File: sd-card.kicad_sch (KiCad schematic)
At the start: 2 parts, among them J7 Micro-SD-card

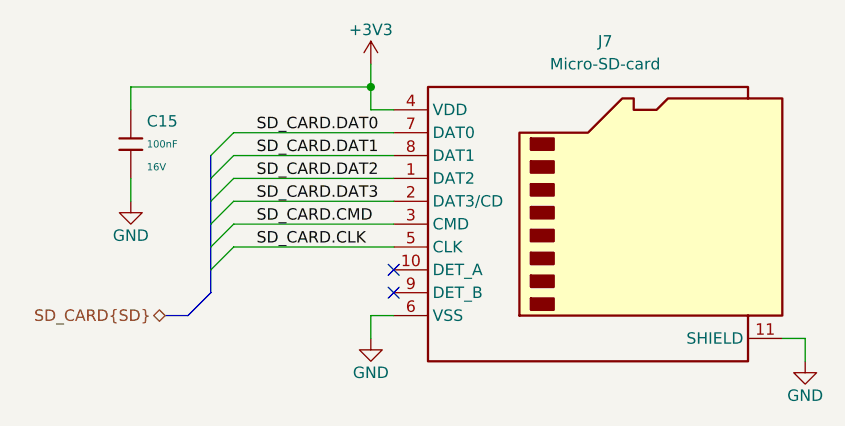
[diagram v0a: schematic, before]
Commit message: [#1] WIP: Change components to ones from the global library, refactor schematic
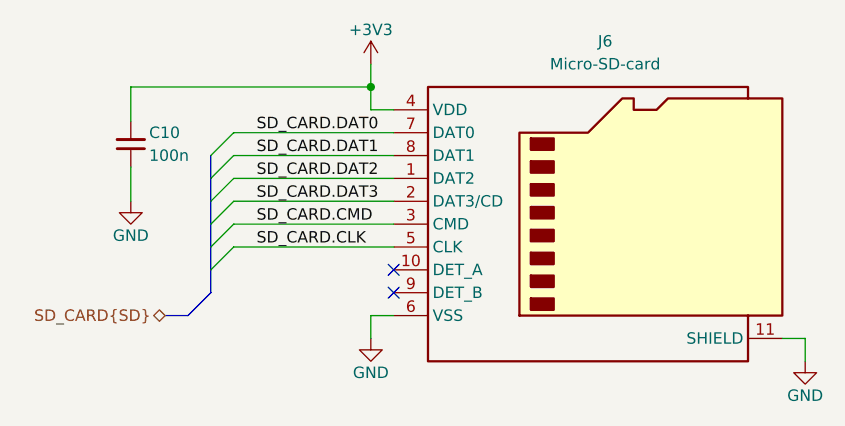
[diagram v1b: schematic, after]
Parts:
- removed C15: 100nF, PCM_JLCPCB:C_0402, symbol PCM_JLCPCB-Capacitors:0402,100nF
- added C10: C-100n-0402, DW-footprints:C_0402_1005Metric, symbol DW-capacitors:C-100n-0402
- renumbered J7 to J6
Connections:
- net +3V3: now also C10.2
- net GND: now also C10.1
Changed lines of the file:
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@@
 	(wire
 		(pts
-			(xy 142.24 113.03) (xy 142.24 115.57)
+			(xy 142.24 113.03) (xy 142.24 116.84)
 		)
 		(stroke
@@
 		)
 	)
+	(wire
+		(pts
+			(xy 142.24 121.92) (xy 142.24 125.73)
+		)
+		(stroke
+			(width 0)
+			(type default)
+		)
+	)
 	(bus
 		(pts
@@
 		(pts
 			(xy 171.45 115.57) (xy 168.91 115.57)
-		)
-		(stroke
-			(width 0)
-			(type default)
-		)
-	)
-	(wire
-		(pts
-			(xy 142.24 123.19) (xy 142.24 125.73)
 		)
 		(stroke
@@
 			)
 			(justify right)
+		)
+	)
+	(symbol
+		(lib_id "DW-capacitors:C-100n-0402")
+		(at 142.24 121.92 90)
+		(unit 1)
+		(exclude_from_sim no)
+		(in_bom yes)
+		(on_board yes)
+		(dnp no)
+		(property "Reference" "C10"
+			(at 144.272 118.11 90)
+			(effects
+				(font
+					(size 1.27 1.27)
+					(thickness 0.15)
+				)
+				(justify right)
+			)
+		)
+		(property "Value" "C-100n-0402"
+			(at 144.78 109.22 0)
+			(effects
+				(font
+					(size 1.27 1.27)
+					(thickness 0.15)
+				)
+				(justify left bottom)
+				(hide yes)
+			)
+		)
+		(property "Footprint" "DW-footprints:C_0402_1005Metric"
+			(at 147.32 109.22 0)
+			(effects
+				(font
+					(size 1.27 1.27)
+					(thickness 0.15)
+				)
+				(justify left bottom)
+				(hide yes)
+			)
+		)
+		(property "Datasheet" "https://lcsc.com/datasheet/lcsc_datasheet_2304140030_Samsung-Electro-Mechanics-CL05B104KB54PNC_C307331.pdf"
+			(at 149.86 109.22 0)
+			(effects
+				(font
+					(size 1.27 1.27)
+					(thickness 0.15)
+				)
+				(justify left bottom)
+				(hide yes)
+			)
+		)
+		(property "Description" "50V 100nF X7R ±10% 0402 Multilayer Ceramic Capacitors MLCC - SMD/SMT ROHS"
+			(at 152.4 109.22 0)
+			(effects
+				(font
+					(size 1.27 1.27)
+					(thickness 0.15)
+				)
+				(justify left bottom)
+				(hide yes)
+			)
+		)
+		(property "Manufacturer" "Samsung Electro-Mechanics"
+			(at 154.94 109.22 0)
+			(effects
+				(font
+					(size 1.27 1.27)
+					(thickness 0.15)
+				)
+				(justify left bottom)
+				(hide yes)
+			)
+		)
+		(property "MPN" "CL05B104KB54PNC"
+			(at 157.48 109.22 0)
+			(effects
+				(font
+					(size 1.27 1.27)
+					(thickness 0.15)
+				)
+				(justify left bottom)
+				(hide yes)
+			)
+		)
+		(property "LCSC" "C307331"
+			(at 160.02 109.22 0)
+			(effects
+				(font
+					(size 1.27 1.27)
+					(thickness 0.15)
+				)
+				(justify left bottom)
+				(hide yes)
+			)
+		)
+		(property "Val" "100n"
+			(at 144.272 120.65 90)
+			(effects
+				(font
+					(size 1.27 1.27)
+					(thickness 0.15)
+				)
+				(justify right)
+			)
+		)
+		(property "Tolerance" "10%"
+			(at 165.1 109.22 0)
+			(effects
+				(font
+					(size 1.27 1.27)
+					(thickness 0.15)
+				)
+				(justify left bottom)
+				(hide yes)
+			)
+		)
+		(property "Voltage" "50V"
+			(at 167.64 109.22 0)
+			(effects
+				(font
+					(size 1.27 1.27)
+					(thickness 0.15)
+				)
+				(justify left bottom)
+				(hide yes)
+			)
+		)
+		(property "Dielectric" "X7R"
+			(at 170.18 109.22 0)
+			(effects
+				(font
+					(size 1.27 1.27)
+					(thickness 0.15)
+				)
+				(justify left bottom)
+				(hide yes)
+			)
+		)
+		(pin "1"
+		)
+		(pin "2"
+		)
+		(instances
+			(project ""
+				(path "/090a8e41-87a8-4fb1-998b-60a2c0dc4cee/df5d742e-fec8-4307-bd86-008404d5e8ea"
+					(reference "C10")
+					(unit 1)
+				)
+			)
 		)
 	)
@@
 		(on_board yes)
 		(dnp no)
-		(property "Reference" "#PWR066"
+		(property "Reference" "#PWR052"
 			(at 217.17 149.86 0)
 			(effects
@@
 			(project "cm5-module"
 				(path "/090a8e41-87a8-4fb1-998b-60a2c0dc4cee/df5d742e-fec8-4307-bd86-008404d5e8ea"
-					(reference "#PWR066")
+					(reference "#PWR052")
 					(unit 1)
 				)
@@
 		(on_board yes)
 		(dnp no)
-		(property "Reference" "#PWR068"
+		(property "Reference" "#PWR049"
 			(at 168.91 114.3 0)
 			(effects
@@
 			(project "cm5-module"
 				(path "/090a8e41-87a8-4fb1-998b-60a2c0dc4cee/df5d742e-fec8-4307-bd86-008404d5e8ea"
-					(reference "#PWR068")
+					(reference "#PWR049")
 					(unit 1)
 				)
@@
 		(on_board yes)
 		(dnp no)
-		(property "Reference" "#PWR067"
+		(property "Reference" "#PWR051"
 			(at 168.91 147.32 0)
 			(effects
@@
 			(project "cm5-module"
 				(path "/090a8e41-87a8-4fb1-998b-60a2c0dc4cee/df5d742e-fec8-4307-bd86-008404d5e8ea"
-					(reference "#PWR067")
+					(reference "#PWR051")
 					(unit 1)
 				)
@@
 		(dnp no)
 		(fields_autoplaced yes)
-		(property "Reference" "J7"
+		(property "Reference" "J6"
 			(at 194.945 107.95 0)
 			(effects
@@
 			(project ""
 				(path "/090a8e41-87a8-4fb1-998b-60a2c0dc4cee/df5d742e-fec8-4307-bd86-008404d5e8ea"
-					(reference "J7")
-					(unit 1)
-				)
-			)
-		)
-	)
-	(symbol
-		(lib_id "PCM_JLCPCB-Capacitors:0402,100nF")
-		(at 142.24 119.38 0)
-		(unit 1)
-		(exclude_from_sim no)
-		(in_bom yes)
-		(on_board yes)
-		(dnp no)
-		(property "Reference" "C15"
-			(at 144.018 116.8399 0)
-			(effects
-				(font
-					(size 1.27 1.27)
-				)
-				(justify left)
-			)
-		)
-		(property "Value" "100nF"
-			(at 144.018 119.38 0)
-			(effects
-				(font
-					(size 0.8 0.8)
-				)
-				(justify left)
-			)
-		)
-		(property "Footprint" "PCM_JLCPCB:C_0402"
-			(at 140.462 119.38 90)
-			(effects
-				(font
-					(size 1.27 1.27)
-				)
-				(hide yes)
-			)
-		)
-		(property "Datasheet" "https://www.lcsc.com/datasheet/lcsc_datasheet_2304140030_Samsung-Electro-Mechanics-CL05B104KO5NNNC_C1525.pdf"
-			(at 142.24 119.38 0)
-			(effects
-				(font
-					(size 1.27 1.27)
-				)
-				(hide yes)
-			)
-		)
-		(property "Description" "16V 100nF X7R ±10% 0402 Multilayer Ceramic Capacitors MLCC - SMD/SMT ROHS"
-			(at 142.24 119.38 0)
-			(effects
-				(font
-					(size 1.27 1.27)
-				)
-				(hide yes)
-			)
-		)
-		(property "LCSC" "C1525"
-			(at 142.24 119.38 0)
-			(effects
-				(font
-					(size 1.27 1.27)
-				)
-				(hide yes)
-			)
-		)
-		(property "Stock" "17504271"
-			(at 142.24 119.38 0)
-			(effects
-				(font
-					(size 1.27 1.27)
-				)
-				(hide yes)
-			)
-		)
-		(property "Price" "0.004USD"
-			(at 142.24 119.38 0)
-			(effects
-				(font
-					(size 1.27 1.27)
-				)
-				(hide yes)
-			)
-		)
-		(property "Process" "SMT"
-			(at 142.24 119.38 0)
-			(effects
-				(font
-					(size 1.27 1.27)
-				)
-				(hide yes)
-			)
-		)
-		(property "Minimum Qty" "20"
-			(at 142.24 119.38 0)
-			(effects
-				(font
-					(size 1.27 1.27)
-				)
-				(hide yes)
-			)
-		)
-		(property "Attrition Qty" "10"
-			(at 142.24 119.38 0)
-			(effects
-				(font
-					(size 1.27 1.27)
-				)
-				(hide yes)
-			)
-		)
-		(property "Class" "Basic Component"
-			(at 142.24 119.38 0)
-			(effects
-				(font
-					(size 1.27 1.27)
-				)
-				(hide yes)
-			)
-		)
-		(property "Category" "Capacitors,Multilayer Ceramic Capacitors MLCC - SMD/SMT"
-			(at 142.24 119.38 0)
-			(effects
-				(font
-					(size 1.27 1.27)
-				)
-				(hide yes)
-			)
-		)
-		(property "Manufacturer" "Samsung Electro-Mechanics"
-			(at 142.24 119.38 0)
-			(effects
-				(font
-					(size 1.27 1.27)
-				)
-				(hide yes)
-			)
-		)
-		(property "Part" "CL05B104KO5NNNC"
-			(at 142.24 119.38 0)
-			(effects
-				(font
-					(size 1.27 1.27)
-				)
-				(hide yes)
-			)
-		)
-		(property "Voltage Rated" "16V"
-			(at 144.018 121.92 0)
-			(effects
-				(font
-					(size 0.8 0.8)
-				)
-				(justify left)
-			)
-		)
-		(property "Tolerance" "±10%"
-			(at 142.24 119.38 0)
-			(effects
-				(font
-					(size 1.27 1.27)
-				)
-				(hide yes)
-			)
-		)
-		(property "Capacitance" "100nF"
-			(at 142.24 119.38 0)
-			(effects
-				(font
-					(size 1.27 1.27)
-				)
-				(hide yes)
-			)
-		)
-		(property "Temperature Coefficient" "X7R"
-			(at 142.24 119.38 0)
-			(effects
-				(font
-					(size 1.27 1.27)
-				)
-				(hide yes)
-			)
-		)
-		(pin "2"
-		)
-		(pin "1"
-		)
-		(instances
-			(project ""
-				(path "/090a8e41-87a8-4fb1-998b-60a2c0dc4cee/df5d742e-fec8-4307-bd86-008404d5e8ea"
-					(reference "C15")
+					(reference "J6")
 					(unit 1)
 				)
@@
 		(on_board yes)
 		(dnp no)
-		(property "Reference" "#PWR069"
+		(property "Reference" "#PWR050"
 			(at 142.24 132.08 0)
 			(effects
@@
 			(project "cm5-module"
 				(path "/090a8e41-87a8-4fb1-998b-60a2c0dc4cee/df5d742e-fec8-4307-bd86-008404d5e8ea"
-					(reference "#PWR069")
+					(reference "#PWR050")
 					(unit 1)
 				)
